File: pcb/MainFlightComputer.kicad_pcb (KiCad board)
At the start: 4 copper layers, 50 x 50 mm, 19 parts, among them J1 USB_B_Micro, J2 ST-Link, U1 STM32H533VET6, U2 MCP2221A-I/ST, U3 AP2112K-3.3

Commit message: Added uSD connector.
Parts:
- added C10: 1u, Capacitor_SMD:C_1206_3216Metric_Pad1.33x1.80mm_HandSolder, F.Cu at (107.8, 92.8)
- added C8: 100n, Capacitor_SMD:C_1206_3216Metric_Pad1.33x1.80mm_HandSolder, F.Cu at (107.8, 86.1)
- added C9: 10n, Capacitor_SMD:C_1206_3216Metric_Pad1.33x1.80mm_HandSolder, F.Cu at (107.8, 89.5)
- added J3: Micro_SD_Card, pcb:microSD_HC_Molex_47219-2001, F.Cu at (150.0, 83.0)
- added R3: R_Small, Resistor_SMD:R_1206_3216Metric_Pad1.30x1.75mm_HandSolder, F.Cu at (101.8, 70.0)
- added R4: R_Small, Resistor_SMD:R_1206_3216Metric_Pad1.30x1.75mm_HandSolder, F.Cu at (101.8, 73.3)
- added R5: R_Small, Resistor_SMD:R_1206_3216Metric_Pad1.30x1.75mm_HandSolder, F.Cu at (101.8, 76.7)
- added R6: R_Small, Resistor_SMD:R_1206_3216Metric_Pad1.30x1.75mm_HandSolder, F.Cu at (101.8, 80.0)
- added R7: R_Small, Resistor_SMD:R_1206_3216Metric_Pad1.30x1.75mm_HandSolder, F.Cu at (101.8, 83.3)
- added R8: R_Small, Resistor_SMD:R_1206_3216Metric_Pad1.30x1.75mm_HandSolder, F.Cu at (101.8, 86.6)
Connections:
- U1 pad 37: unconnected-(U1-PB2-Pad37) -> SD_CMD
- U1 pad 52: unconnected-(U1-PB13-Pad52) -> SD_DAT0
- U1 pad 66: unconnected-(U1-PC9-Pad66) -> SD_DAT1
- U1 pad 78: unconnected-(U1-PC10-Pad78) -> SD_DAT2
- U1 pad 79: unconnected-(U1-PC11-Pad79) -> SD_DAT3
- U1 pad 80: unconnected-(U1-PC12-Pad80) -> SD_CLK

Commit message: Formalizing a debug header.
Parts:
- J2: value ST-Link -> Debug; footprint Connector_IDC:IDC-Header_2x05_P2.54mm_Horizontal -> pcb:Molex_PicoBlade_53047-1010_1x10_P1.25mm_Vertical
- moved J2 4.63 mm to (155.6, 122.0), turned to 180 degrees
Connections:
- J2 pad 1: RESET -> +3.3V
- J2 pad 10: +5V -> GND
- J2 pad 2: SWCLK -> GND
- J2 pad 3: unconnected-(J2-Pin_3-Pad3) -> RESET
- J2 pad 4: SWDIO -> SWCLK
- J2 pad 5: GND -> STLINK_TX
- J2 pad 6: GND -> SWDIO
- J2 pad 7: +3.3V -> STLINK_RX
- J2 pad 8: +3.3V -> SWO
- J2 pad 9: +5V -> GND
- U1 pad 25: /USB_UART_Bridge/SERIAL_OUT -> STLINK_TX
- U1 pad 26: /USB_UART_Bridge/SERIAL_IN -> STLINK_RX
- U1 pad 29: /USB_UART_Bridge/SERIAL_RESET -> unconnected-(U1-PA4-Pad29)
- U1 pad 89: unconnected-(U1-PB3(JTDO-Pad89) -> SWO

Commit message: Trying out design blocks instead of hierarchal sheets.
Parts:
- C1: value 10u -> 2u2
- C10, C3: value 1u -> 100n
- C2: value 1u -> 2u2
- C4, C8: value 100n -> 1u
- C6: value 2u2 -> 10n
- C7: value 2u2 -> 10u
- C9: value 10n -> 1u
- JP1: value Jumper_2_Small_Bridged -> Jumper_3_Bridged12; footprint Connector_PinHeader_2.54mm:PinHeader_1x02_P2.54mm_Vertical -> Connector_PinHeader_2.54mm:PinHeader_1x03_P2.54mm_Vertical
- JP2: value Jumper_3_Bridged12 -> Jumper_2_Small_Bridged; footprint Connector_PinHeader_2.54mm:PinHeader_1x03_P2.54mm_Vertical -> Connector_PinHeader_2.54mm:PinHeader_1x02_P2.54mm_Vertical
- R1, R2: value 2K -> R_Small
- R7, R8: value R_Small -> 2K
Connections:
- net /USB_UART_Bridge/SERIAL_IN renamed SERIAL_IN
- net /USB_UART_Bridge/SERIAL_IN_ACTIVITY renamed /SERIAL_IN_ACTIVITY
- net /USB_UART_Bridge/SERIAL_OUT renamed SERIAL_OUT
- net /USB_UART_Bridge/SERIAL_OUT_ACTIVITY renamed /SERIAL_OUT_ACTIVITY
- net /USB_UART_Bridge/SERIAL_RESET renamed SERIAL_RESET
- net /USB_UART_Bridge/USB_D+ renamed /USB_D+
- net /USB_UART_Bridge/USB_D- renamed /USB_D-
- C1 pad 1: Net-(J1-VBUS) -> Net-(C1-Pad1)
- C2 pad 1: Net-(J1-VBUS) -> Net-(C1-Pad1)
- C6 pad 1: Net-(C6-Pad1) -> +3.3V
- C7 pad 1: Net-(C6-Pad1) -> Net-(J1-VBUS)
- C8 pad 1: +3.3V -> Net-(J1-VBUS)
- JP1 pad 1: Net-(J1-VBUS) -> GND
- JP1 pad 2: /USB_UART_Bridge/PWR_BY_USB_EN -> /BOOT0
- JP2 pad 1: GND -> Net-(J1-VBUS)
- JP2 pad 2: /BOOT0 -> /PWR_BY_USB_EN
- R1 pad 1: +3.3V -> SD_DAT2
- R1 pad 2: Net-(D1-A) -> Net-(J3-DAT2)
- R2 pad 1: Net-(D2-A) -> SD_CLK
- R2 pad 2: +3.3V -> Net-(J3-CLK)
- R3 pad 1: SD_DAT2 -> SD_DAT0
- R3 pad 2: Net-(J3-DAT2) -> Net-(J3-DAT0)
- R5 pad 1: SD_CMD -> SD_DAT1
- R5 pad 2: Net-(J3-CMD) -> Net-(J3-DAT1)
- R6 pad 1: SD_CLK -> SD_CMD
- R6 pad 2: Net-(J3-CLK) -> Net-(J3-CMD)
- R7 pad 1: SD_DAT0 -> +3.3V
- R7 pad 2: Net-(J3-DAT0) -> Net-(D1-A)
- R8 pad 1: SD_DAT1 -> Net-(D2-A)
- R8 pad 2: Net-(J3-DAT1) -> +3.3V
- U1 pad 48: Net-(C6-Pad1) -> Net-(C1-Pad1)
- U1 pad 98: Net-(C6-Pad1) -> Net-(C1-Pad1)
- U3 pad 3: /USB_UART_Bridge/PWR_BY_USB_EN -> /PWR_BY_USB_EN

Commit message: Added debug buzzer.
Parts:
- added BZ1: AST1109MLTRQ, Buzzer_Beeper:Buzzer_Mallory_AST1109MLTRQ, F.Cu at (133.5, 117.5)
- added BZ2: WT-1205, Buzzer_Beeper:MagneticBuzzer_ProSignal_ABT-410-RC, F.Cu at (133.5, 114.2)
- added JP3: Jumper_3_Bridged12, Connector_PinHeader_2.54mm:PinHeader_1x03_P2.54mm_Vertical, F.Cu at (211.5, 102.4)
- added R10: 50, Resistor_SMD:R_1206_3216Metric_Pad1.30x1.75mm_HandSolder, F.Cu at (206.2, 105.1)
- added R9: 100, Resistor_SMD:R_1206_3216Metric_Pad1.30x1.75mm_HandSolder, F.Cu at (206.2, 101.8)

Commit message: Added pinouts for peripherals.
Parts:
- added J4: Pinout, Connector_IDC:IDC-Header_2x17_P2.54mm_Horizontal, F.Cu at (129.2, 120.3)
- moved BZ1 36.5 mm to (167.4, 104.0)
- moved BZ2 36.5 mm to (167.4, 100.8)
- moved C5 11.7 mm to (105.0, 102.5)
- moved C6 11.7 mm to (105.0, 105.8)
- moved C7 11.7 mm to (105.0, 109.2)
- moved JP2 11.7 mm to (104.3, 113.2)

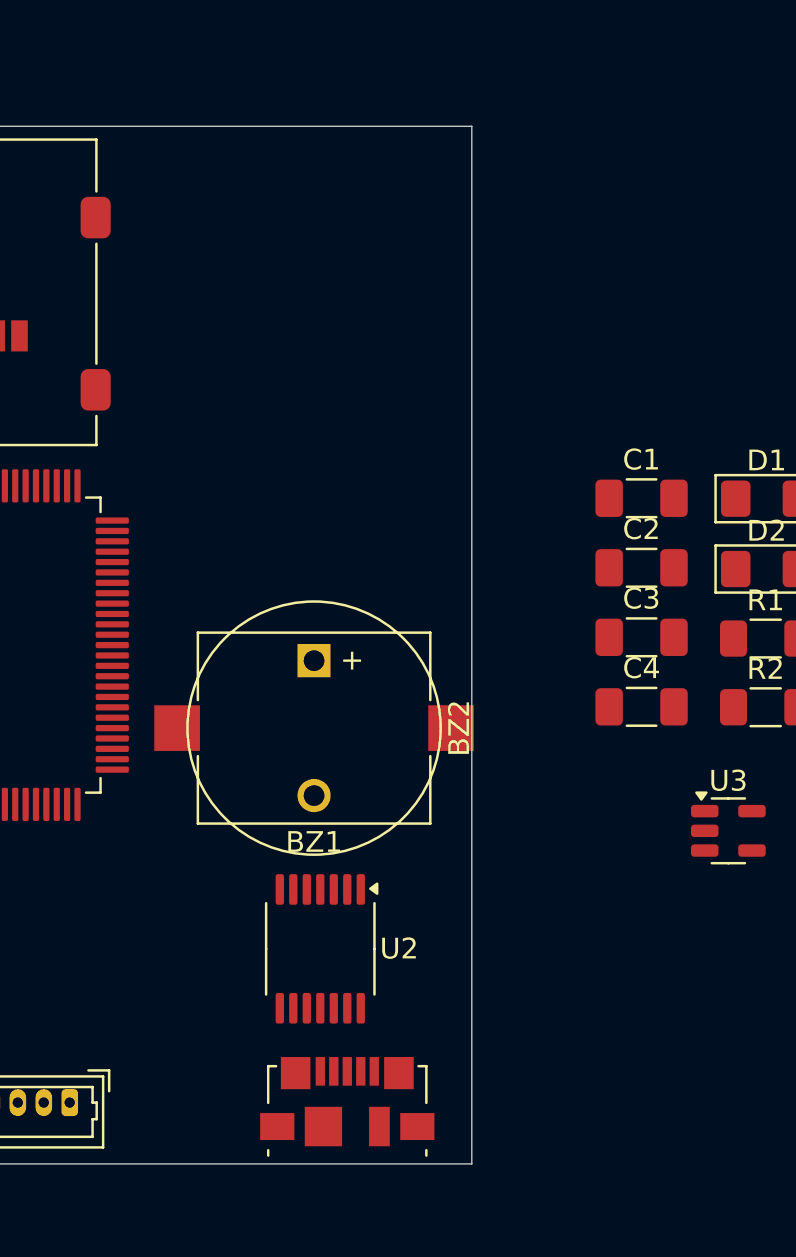
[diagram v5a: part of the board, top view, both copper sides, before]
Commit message: Made debug LED.
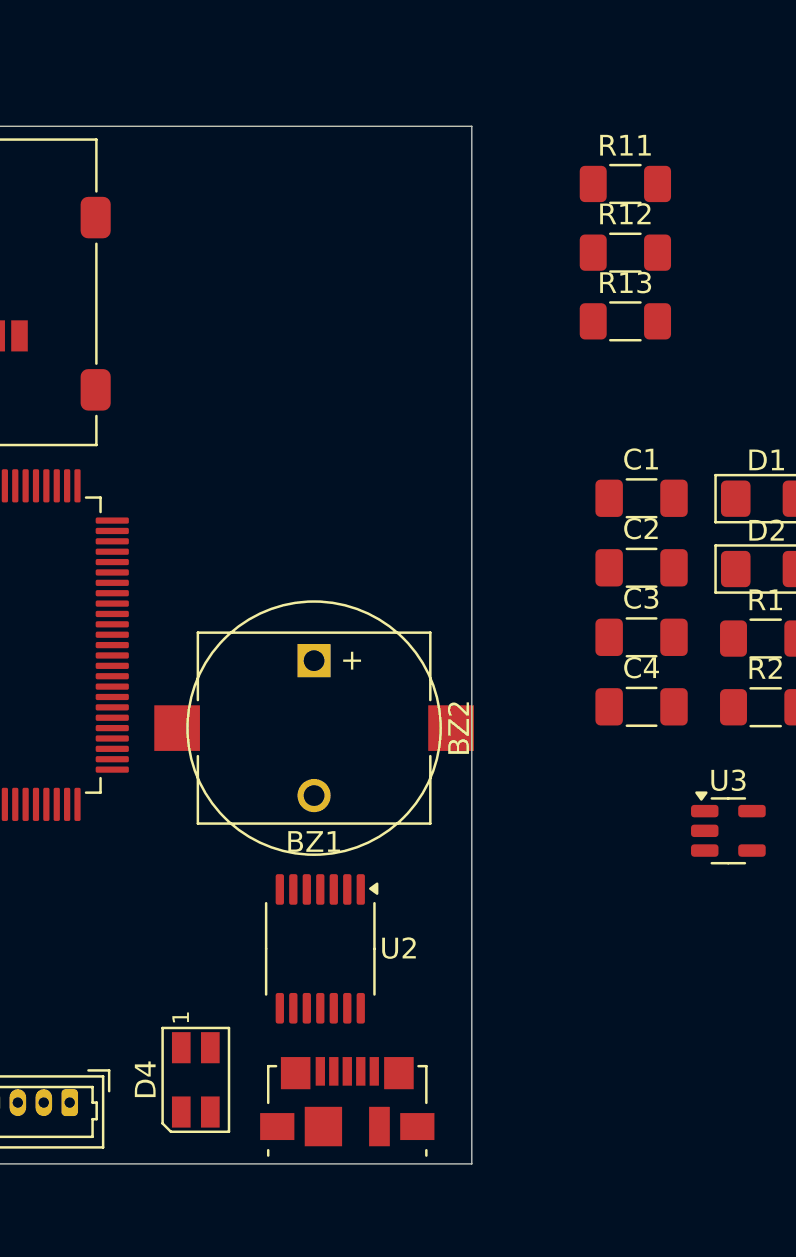
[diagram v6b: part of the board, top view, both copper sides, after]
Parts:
- added D4: 150141M173100, LED_SMD:LED_RGB_Wuerth-PLCC4_3.2x2.8mm_150141M173100, F.Cu at (161.7, 121.0)
- added R11: 2K, Resistor_SMD:R_1206_3216Metric_Pad1.30x1.75mm_HandSolder, F.Cu at (182.4, 77.8)
- added R12: 2K, Resistor_SMD:R_1206_3216Metric_Pad1.30x1.75mm_HandSolder, F.Cu at (182.4, 81.1)
- added R13: 2K, Resistor_SMD:R_1206_3216Metric_Pad1.30x1.75mm_HandSolder, F.Cu at (182.4, 84.4)

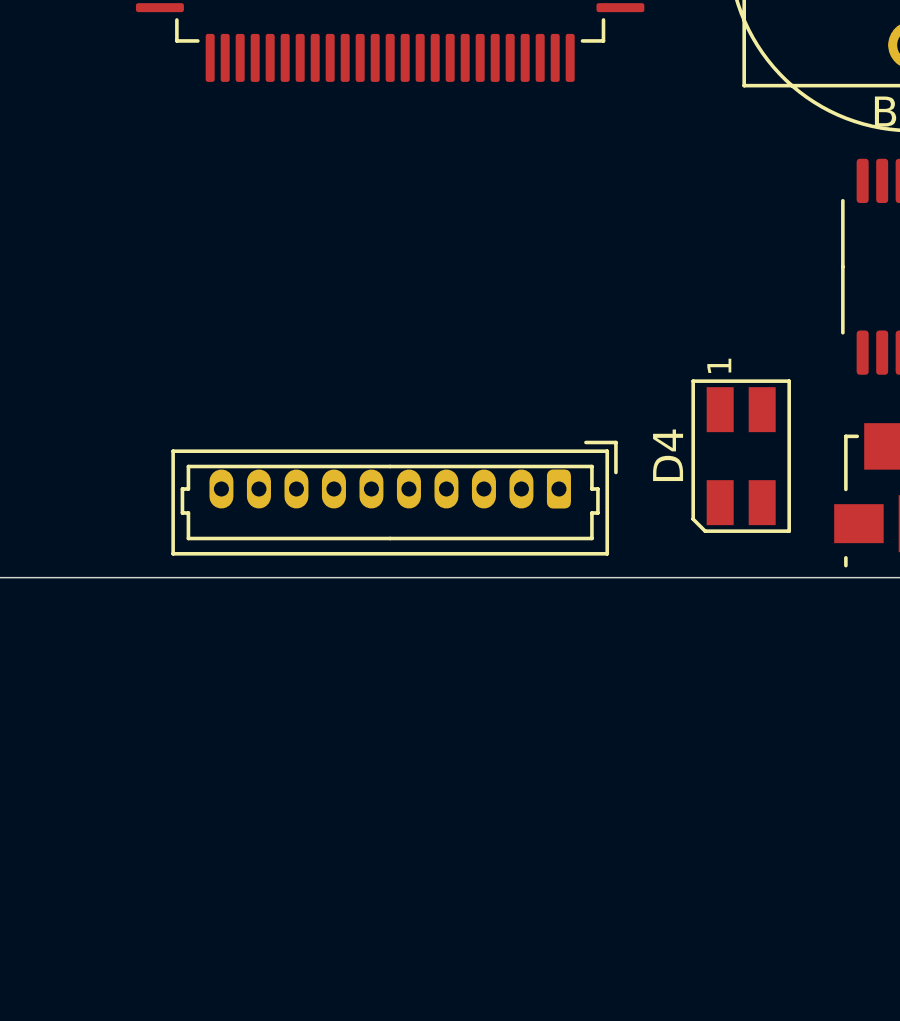
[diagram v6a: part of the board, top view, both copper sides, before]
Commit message: Updated the USB-UART bridge to have LEDs to indicate VBUS and +3.3V.
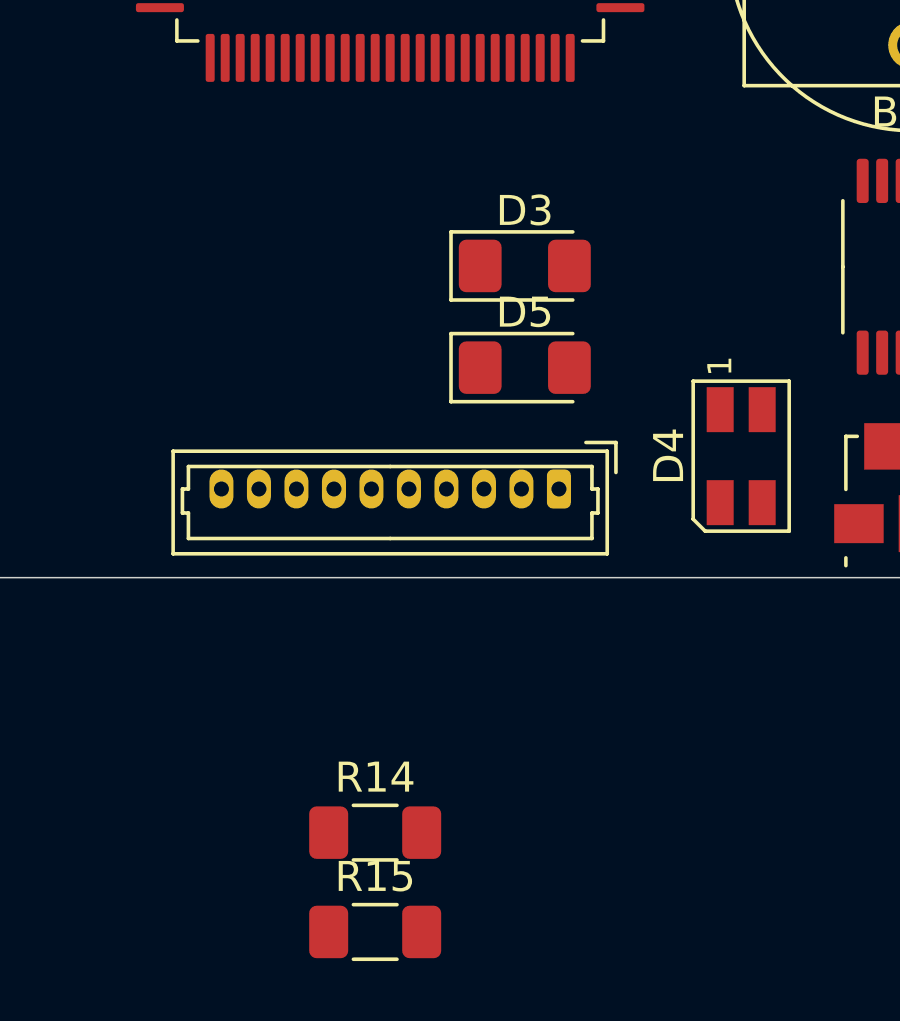
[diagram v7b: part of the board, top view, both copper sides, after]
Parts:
- added D3: GREEN, LED_SMD:LED_1206_3216Metric_Pad1.42x1.75mm_HandSolder, F.Cu at (154.5, 114.6)
- added D5: GREEN, LED_SMD:LED_1206_3216Metric_Pad1.42x1.75mm_HandSolder, F.Cu at (154.5, 118.0)
- added R14: 4K, Resistor_SMD:R_1206_3216Metric_Pad1.30x1.75mm_HandSolder, F.Cu at (149.5, 133.5)
- added R15: 4K, Resistor_SMD:R_1206_3216Metric_Pad1.30x1.75mm_HandSolder, F.Cu at (149.5, 136.8)

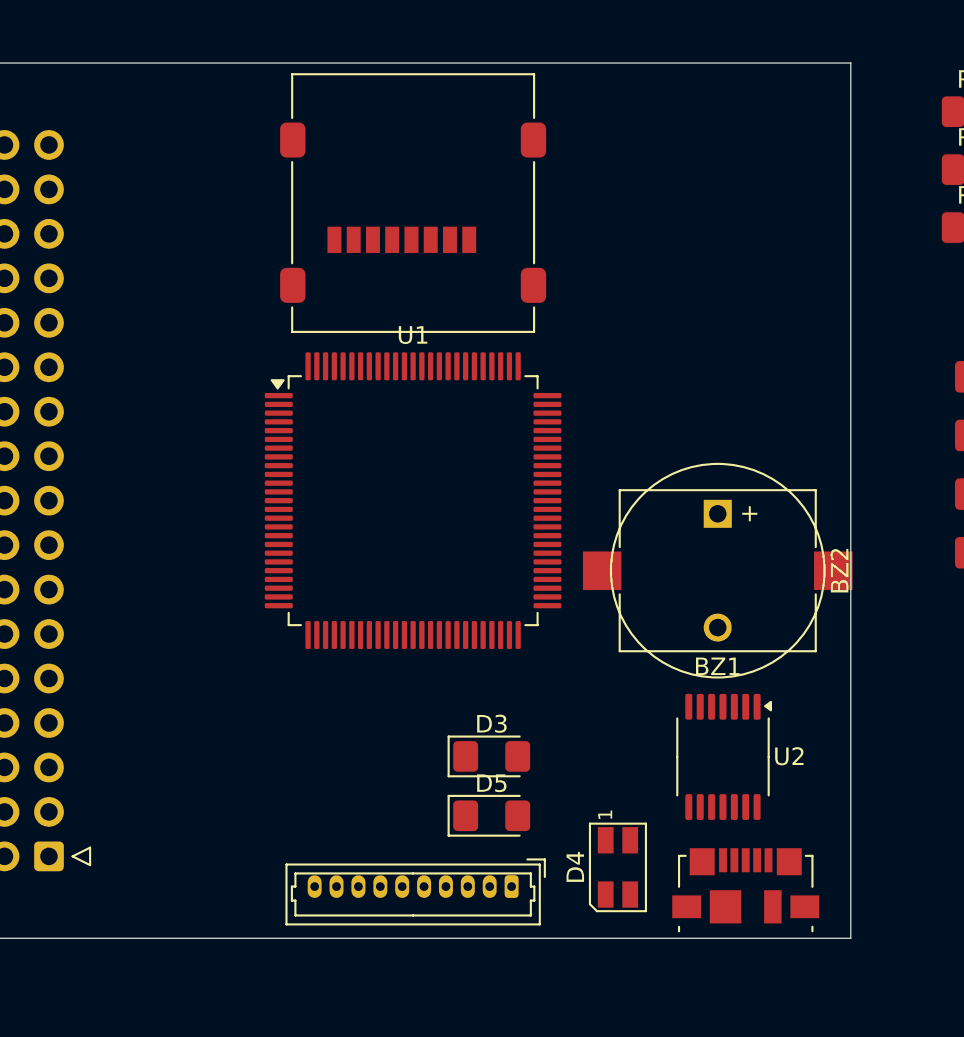
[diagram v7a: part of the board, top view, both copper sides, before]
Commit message: Added mounting holes.
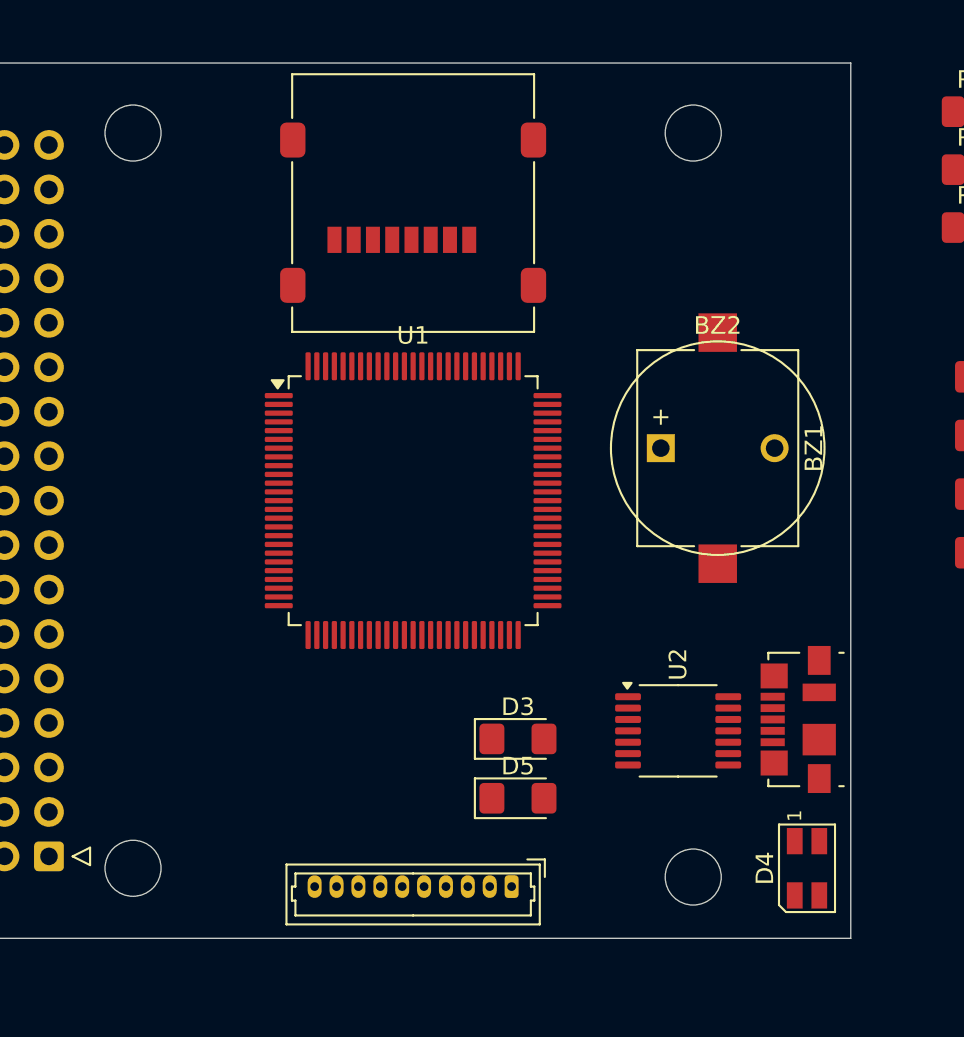
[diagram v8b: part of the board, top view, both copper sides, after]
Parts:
- added H1: M3, MountingHole:MountingHole_3.2mm_M3, F.Cu at (134.0, 121.0)
- added H2: M3, MountingHole:MountingHole_3.2mm_M3, F.Cu at (166.0, 121.5)
- added H3: M3, MountingHole:MountingHole_3.2mm_M3, F.Cu at (166.0, 79.0)
- added H4: M3, MountingHole:MountingHole_3.2mm_M3, F.Cu at (134.0, 79.0)
- moved D4 10.8 mm to (172.5, 121.0)
- moved J1 9.96 mm to (172.0, 112.5), turned to 90 degrees
- moved BZ1 7.00 mm to (167.4, 97.0), turned to 90 degrees
- moved BZ2 4.96 mm to (164.2, 97.0), turned to 0 degrees
- moved U2 2.96 mm to (165.1, 113.2), turned to 0 degrees
- moved D3 1.80 mm to (156.0, 113.6)
- moved D5 1.80 mm to (156.0, 117.0)
